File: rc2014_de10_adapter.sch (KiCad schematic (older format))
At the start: 27 parts, among them J1 Conn_02x20_Odd_Even, J2 Conn_01x10_Male, J3 Conn_01x08_Male, J4 M3 Mounting Hole, J5 Z80 Bus, J6 Pro Bus, U1 SN74LVC245A, U10 MAX40200AUK, U2 SN74LVC245A, U3 SN74LVC245A, U4 SN74LVC245A, U5 SN74LVC245A, U6 AZ1117-3.3, U7 MAX40200AUK, U8 MAX40200AUK, U9 MAX40200AUK

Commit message: finished routing
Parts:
- removed C4: 100nF, Capacitor_SMD:C_0805_2012Metric_Pad1.15x1.40mm_HandSolder, symbol Device:C
- removed C6: 1uF, Capacitor_SMD:C_0805_2012Metric_Pad1.15x1.40mm_HandSolder, symbol Device:C
- removed U7, U8: MAX40200AUK, Package_TO_SOT_SMD:SOT-23-5, symbol Analog_Switch:MAX40200AUK
- added C1, C3, C8: 100nF, Capacitor_SMD:C_0805_2012Metric_Pad1.15x1.40mm_HandSolder, symbol Device:C
- C5: value 1uF -> 100nF
- renumbered C9 to C10, C10 to C12, C1 to C4, C3 to C6, C8 to C9, J5 to J1, J6 to J2, J4 to J3, J2 to J4, J1 to J5, J3 to J6, U6 to U1, U9 to U2, U5 to U3, U1 to U4, U2 to U5, U10 to U6, U3 to U7, U4 to U8
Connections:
- net +3V3: now also C4.2, C5.2, C7.2, C3.2, C8.2
- net +5V: now also C1.2; no longer C4.2, C5.2, C7.2
- net A0F: now also J5.7 (Pin_7); no longer J5.28 (Pin_28)
- net A10F: now also J5.15 (Pin_15); no longer J5.23 (Pin_23)
- net A11F: now also J5.16 (Pin_16); no longer J5.21 (Pin_21)
- net A12F: now also J5.13 (Pin_13); no longer J5.19 (Pin_19)
- net A13F: now also J5.14 (Pin_14); no longer J5.17 (Pin_17)
- net A14F: now also J5.9 (Pin_9); no longer J5.15 (Pin_15)
- net A15F: now also J5.10 (Pin_10); no longer J5.13 (Pin_13)
- net A1F: now also J5.8 (Pin_8); no longer J5.26 (Pin_26)
- net A2F: now also J5.5 (Pin_5); no longer J5.24 (Pin_24)
- net A3F: now also J5.6 (Pin_6); no longer J5.22 (Pin_22)
- net A4F: now also J5.3 (Pin_3); no longer J5.20 (Pin_20)
- net A5F: now also J5.4 (Pin_4); no longer J5.18 (Pin_18)
- net A6F: now also J5.1 (Pin_1); no longer J5.16 (Pin_16)
- net A7F: now also J5.2 (Pin_2); no longer J5.14 (Pin_14)
- net A8F: now also J5.17 (Pin_17); no longer J5.27 (Pin_27)
- net A9F: now also J5.18 (Pin_18); no longer J5.25 (Pin_25)
- net CLKF: now also J5.21 (Pin_21); no longer J5.3 (Pin_3)
- net D0F: now also J5.33 (Pin_33); no longer J5.31 (Pin_31)
- net D1F: now also J5.34 (Pin_34); no longer J5.33 (Pin_33)
- net D3F: now also J5.36 (Pin_36); no longer J5.37 (Pin_37)
- net D4F: now also J5.37 (Pin_37); no longer J5.32 (Pin_32)
- net D5F: now also J5.38 (Pin_38); no longer J5.34 (Pin_34)
- net D6F: now also J5.39 (Pin_39); no longer J5.36 (Pin_36)
- net D7F: now also J5.40 (Pin_40); no longer J5.38 (Pin_38)
- net DIR: now also J6.6 (Pin_6); no longer J6.8 (Pin_8)
- net GND: now also J4.4 (Pin_4), C1.1, C3.1, C8.1; no longer J4.7 (Pin_7)
- net PAGE: now also U8.2 (A1); no longer U8.8 (A7)
- net PAGEF: now also J4.5 (Pin_5), U8.18 (B1); no longer J4.9 (Pin_9), U8.12 (B7)
- net RxF: now also J6.7 (Pin_7); no longer J6.1 (Pin_1)
- net TxF: now also J6.8 (Pin_8); no longer J6.2 (Pin_2)
- net ~BUSACKF: now also J6.4 (Pin_4); no longer J5.4 (Pin_4)
- net ~BUSRQ: now also U8.7 (A6); no longer U8.3 (A2)
- net ~BUSRQF: now also J6.2 (Pin_2), U8.13 (B6); no longer J5.8 (Pin_8), U8.17 (B2)
- net ~HALT: now also U8.6 (A5); no longer U8.2 (A1)
- net ~HALTF: now also J6.1 (Pin_1), U8.14 (B5); no longer J5.6 (Pin_6), U8.18 (B1)
- net ~INT: now also U8.3 (A2); no longer U8.6 (A5)
- net ~INTF: now also J4.7 (Pin_7), U8.17 (B2); no longer J5.40 (Pin_40), U8.14 (B5)
- net ~IORQF: now also J5.27 (Pin_27); no longer J5.2 (Pin_2)
- net ~M1F: now also J5.19 (Pin_19); no longer J5.1 (Pin_1)
- net ~MREQF: now also J5.23 (Pin_23); no longer J5.5 (Pin_5)
- net ~NMIF: now also J4.8 (Pin_8); no longer J5.10 (Pin_10)
- net ~RDF: now also J5.24 (Pin_24); no longer J5.9 (Pin_9)
- net ~RESETF: now also J5.22 (Pin_22); no longer J4.10 (Pin_10)
- net ~WAIT: now also U8.8 (A7); no longer U8.7 (A6)
- net ~WAITF: now also J6.3 (Pin_3), U8.12 (B7); no longer J5.39 (Pin_39), U8.13 (B6)
- net ~WRF: now also J5.25 (Pin_25); no longer J5.7 (Pin_7)
- net 5VF: no longer names the net of J5.11 (Pin_11)
- no-connect marks 17 -> 18
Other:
- moved on the sheet: C4, J6

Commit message: Added FTDI header
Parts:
- added J7: FTDI, Connector_PinHeader_2.54mm:PinHeader_1x06_P2.54mm_Horizontal, symbol Connector_Generic:Conn_01x06
- added JP1: Jumper, Connector_PinHeader_2.54mm:PinHeader_1x02_P2.54mm_Vertical, symbol Device:Jumper
- added R1, R2, R3, R4: 2k2, Resistor_SMD:R_0805_2012Metric_Pad1.15x1.40mm_HandSolder, symbol Device:R_Small
- added R5, R6: 100K, Resistor_SMD:R_0805_2012Metric_Pad1.15x1.40mm_HandSolder, symbol Device:R_Small
- J4: symbol Connector:Conn_01x10_Male -> Connector_Generic:Conn_01x10
- J6: symbol Connector:Conn_01x08_Male -> Connector_Generic:Conn_01x08
- U1: MFR (none) -> Diodes Incorporated; MPN (none) -> AZ1117H-3.3TRE1; SPN (none) -> 621-AZ1117H-3.3TRE1; SPR (none) -> Mouser; SPURL (none) -> https://www.mouser.com/ProductDetail/Diodes-Incorporated/AZ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
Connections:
- net +3V3: now also JP1.1, R5.1
- net DIR: now also J6.4 (Pin_4); no longer J6.6 (Pin_6)
- net GND: now also J7.1 (Pin_1), R6.2
- net RxF: now also R1.1
- net TxF: now also R2.1
- net ~BUSACKF: now also J6.2 (Pin_2); no longer J6.4 (Pin_4)
- net ~BUSRQF: now also J4.10 (Pin_10); no longer J6.2 (Pin_2)
- net ~HALTF: now also J4.9 (Pin_9); no longer J6.1 (Pin_1)
- net ~WAITF: now also J6.1 (Pin_1); no longer J6.3 (Pin_3)
- net ~CTSF: now reaches J6.5 (Pin_5)
- net ~CTSF: now also R4.1
- new net: J7.2 (Pin_2), R3.2
- new net: J7.3 (Pin_3), JP1.2
- new net: J7.4 (Pin_4), R1.2, R5.2
- new net: J7.5 (Pin_5), R2.2
- new net: J7.6 (Pin_6), R4.2, R6.1
- new net ~RTSF: J6.6 (Pin_6), R3.1
- no-connect marks 18 -> 16

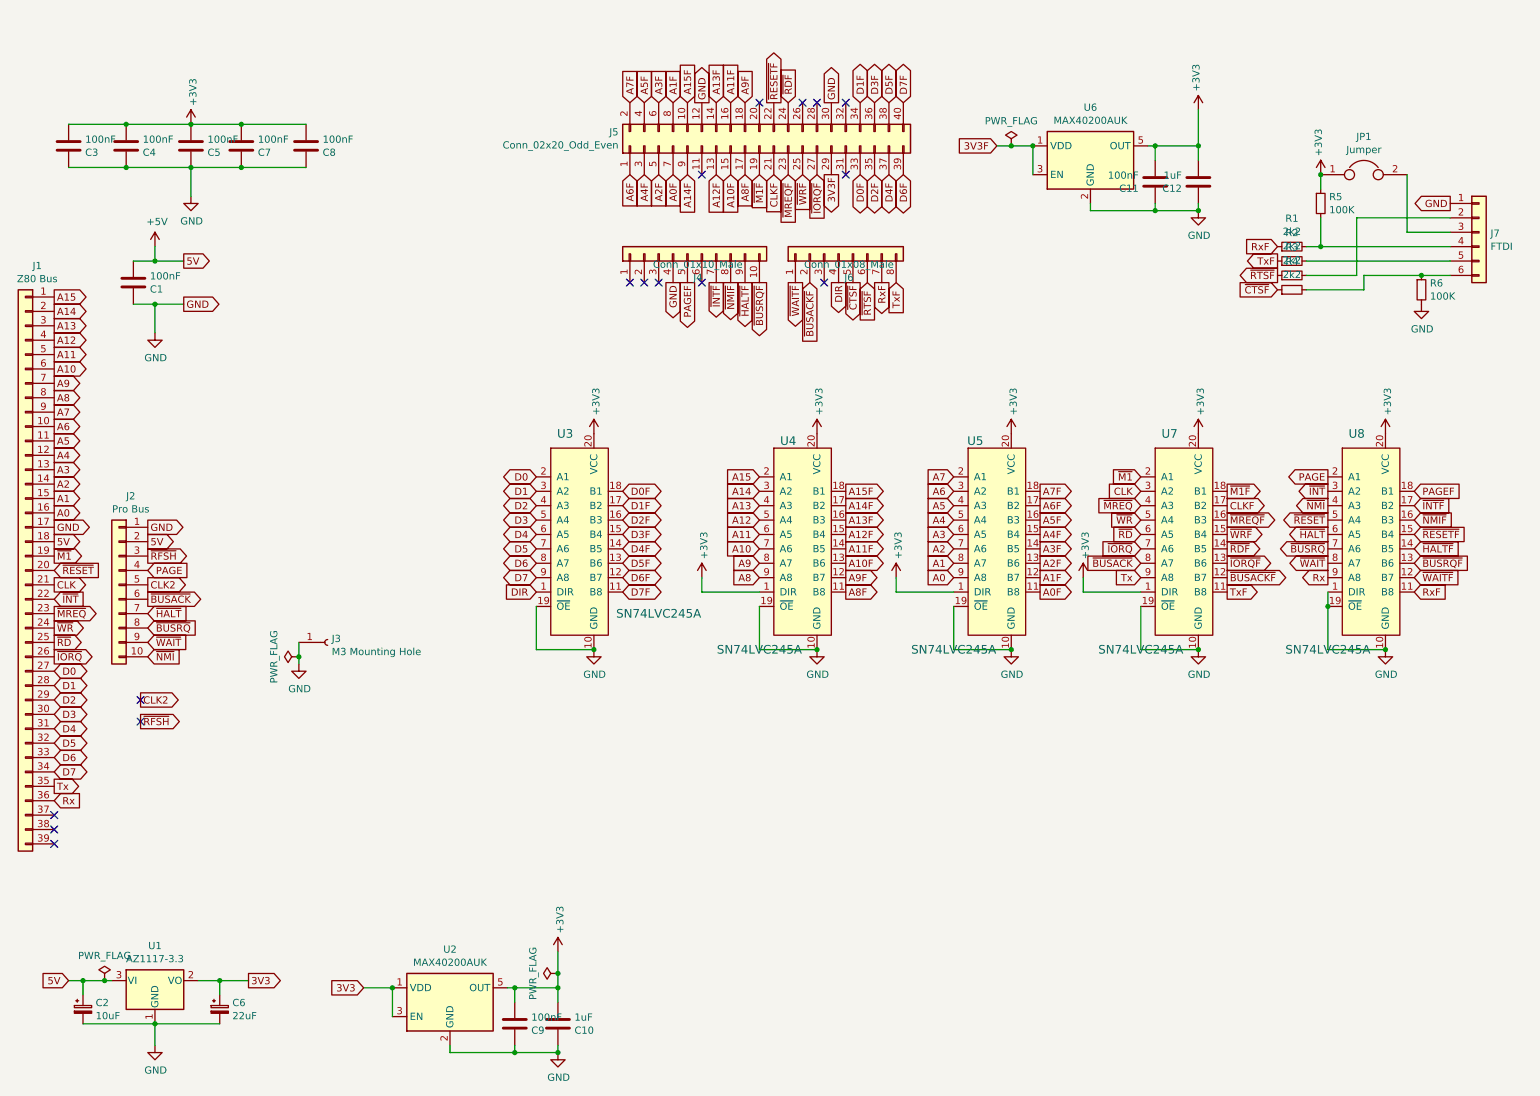
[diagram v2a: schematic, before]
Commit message: added direction flags for bus transceivers
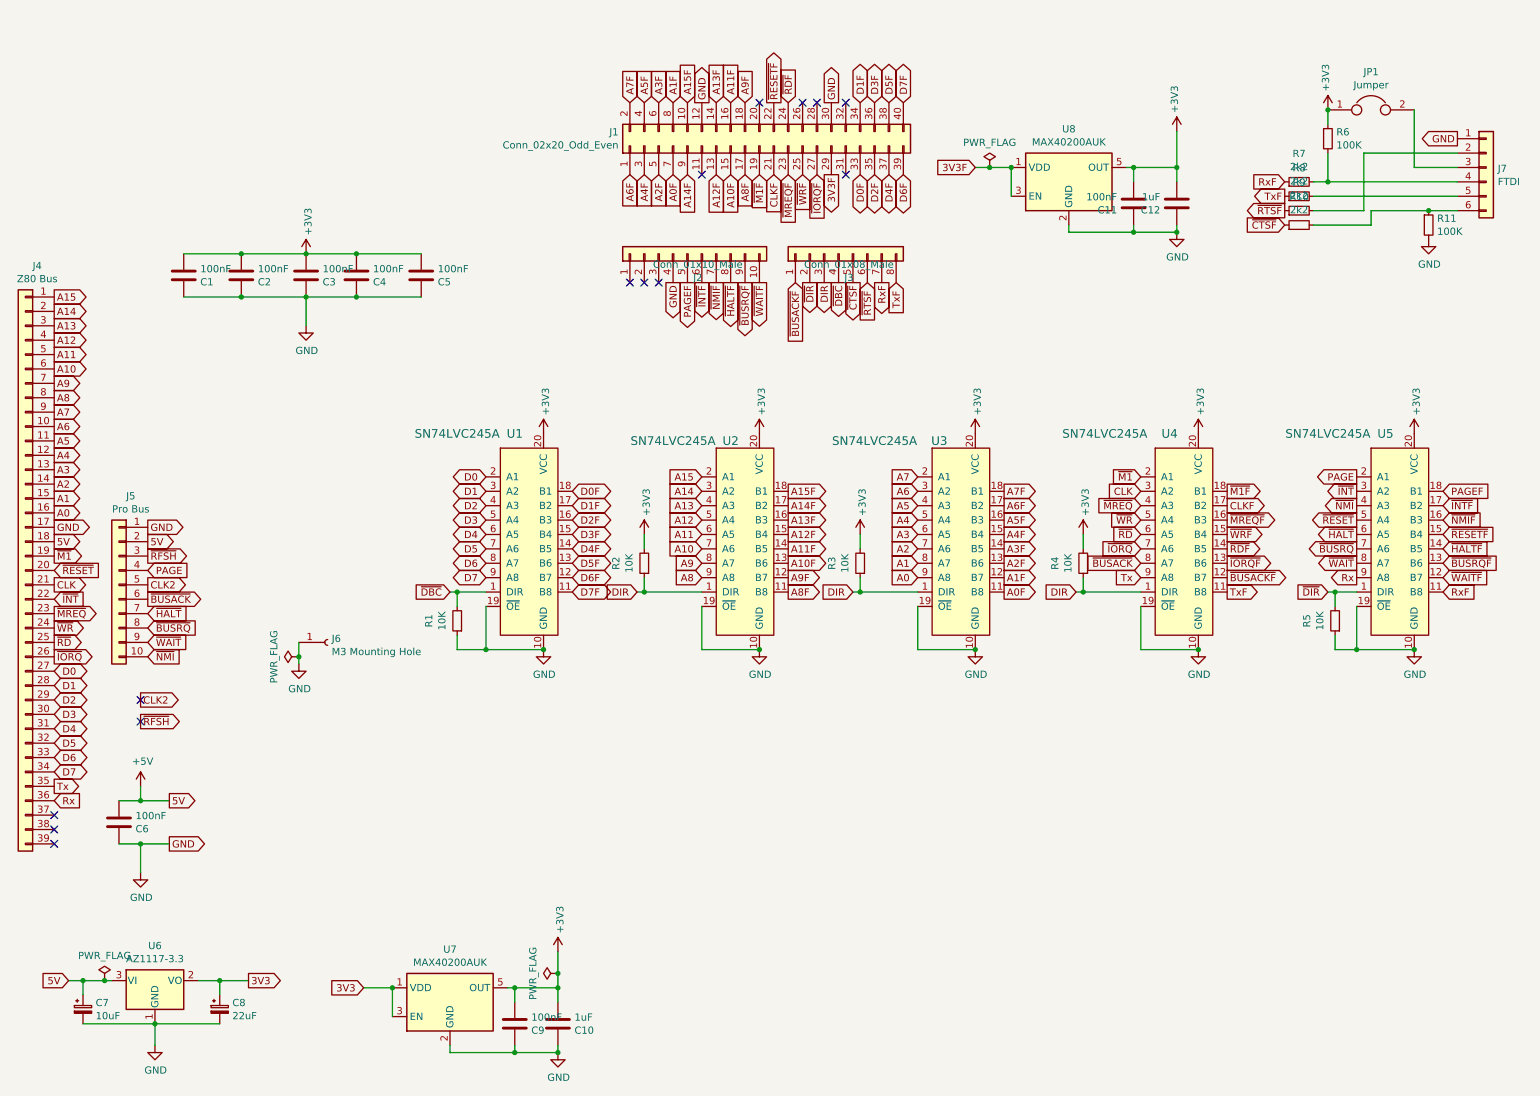
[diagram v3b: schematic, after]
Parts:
- added R1, R2, R3, R4, R5: 10K, Resistor_SMD:R_0805_2012Metric_Pad1.15x1.40mm_HandSolder, symbol Device:R_Small
- renumbered C3 to C1, C4 to C2, C5 to C3, C7 to C4, C8 to C5, C1 to C6, C2 to C7, C6 to C8, J5 to J1, J4 to J2, J6 to J3, J1 to J4, J2 to J5, J3 to J6, R4 to R10, R6 to R11, R5 to R6, R1 to R7, R2 to R8, R3 to R9, U3 to U1, U4 to U2, U5 to U3, U7 to U4, U8 to U5, U1 to U6, U2 to U7, U6 to U8
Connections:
- net +3V3: now also R2.2, R3.2, R4.2; no longer U2.1 (DIR), U3.1 (DIR), U4.1 (DIR)
- net DIR: now also J3.3 (Pin_3), U2.1 (DIR), U3.1 (DIR), U4.1 (DIR), R2.1, R3.1, R4.1; no longer J3.4 (Pin_4), U1.1 (DIR)
- net GND: now also R1.1, R5.1; no longer U5.1 (DIR)
- net ~BUSACKF: now also J3.1 (Pin_1); no longer J3.2 (Pin_2)
- net ~BUSRQF: now also J2.9 (Pin_9); no longer J2.10 (Pin_10)
- net ~HALTF: now also J2.8 (Pin_8); no longer J2.9 (Pin_9)
- net ~INTF: now also J2.6 (Pin_6); no longer J2.7 (Pin_7)
- net ~NMIF: now also J2.7 (Pin_7); no longer J2.8 (Pin_8)
- net ~WAITF: now also J2.10 (Pin_10); no longer J3.1 (Pin_1)
- new net ~DBC: J3.4 (Pin_4), R1.2, U1.1 (DIR)
- new net ~DIR: J3.2 (Pin_2), R5.2, U5.1 (DIR)
- no-connect marks 16 -> 14
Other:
- moved on the sheet: C1, C11, C12, C2, C3, C4, C5, C6, J7, JP1, R10, R11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

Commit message: fix caps on ideal diodes
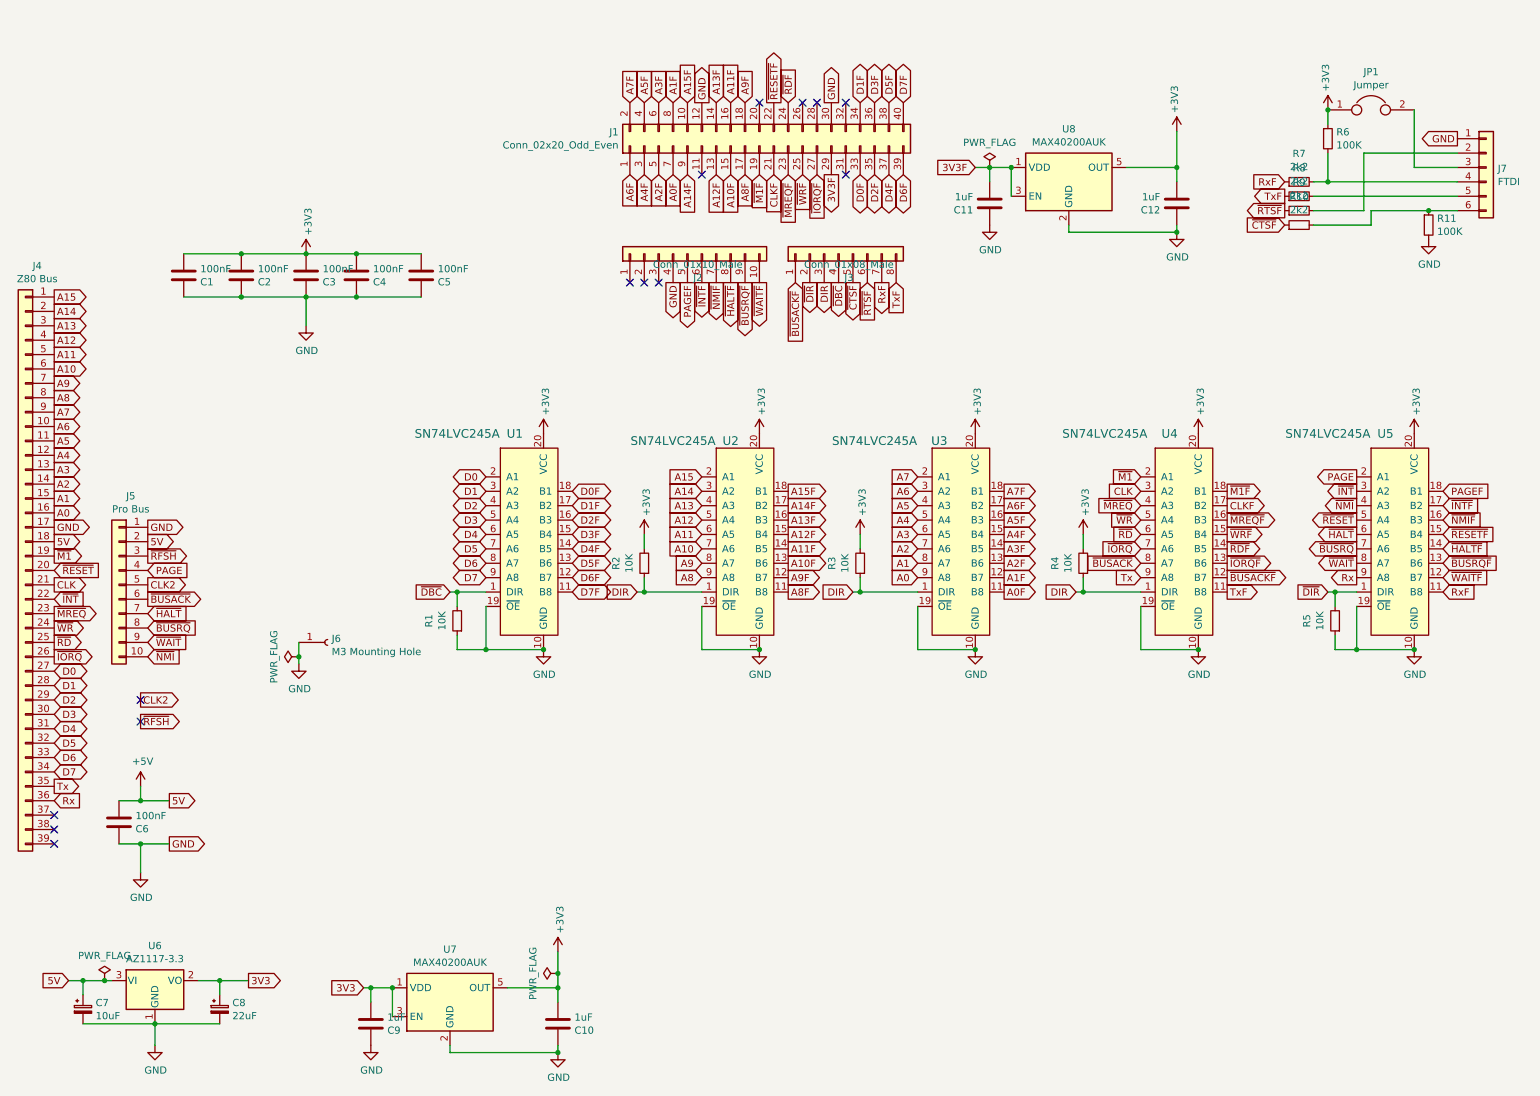
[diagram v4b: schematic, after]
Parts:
- C11, C9: value 100nF -> 1uF
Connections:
- net +3V3: no longer C11.2, C9.2
- net 3V3: now also C9.2
- net 3V3F: now also C11.2
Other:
- moved on the sheet: C11, C9
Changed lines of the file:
@@
 $EndComp
 Wire Wire Line
-	3100 7050 3300 7050
+	3100 7050 3150 7050
 Wire Wire Line
 	7600 1350 7600 1550
@@
 L Device:C C9
 U 1 1 5CD7F41A
-P 4150 7300
-F 0 "C9" H 4265 7346 50  0000 L CNN
-F 1 "100nF" H 4265 7255 50  0000 L CNN
-F 2 "Capacitor_SMD:C_0805_2012Metric_Pad1.15x1.40mm_HandSolder" H 4188 7150 50  0001 C CNN
-F 3 "https://www.mouser.com/datasheet/2/212/KEM_C1002_X7R_SMD-1102033.pdf" H 4150 7300 50  0001 C CNN
-F 4 "KEMET" H -1150 600 50  0001 C CNN "MFR"
-F 5 "C0805C104K4RACTU" H -1150 600 50  0001 C CNN "MPN"
-F 6 "Mouser" H -1150 600 50  0001 C CNN "SPR"
-F 7 "80-C0805C104K4R" H -1150 600 50  0001 C CNN "SPN"
-F 8 "https://www.mouser.com/ProductDetail/KEMET/C0805C104K4RACTU?qs=sGAEpiMZZMs0AnBnWHyRQFCCI5cSbRT%2F1Gdrl2EbPVM%3D" H -1150 600 50  0001 C CNN "SPURL"
-	1    4150 7300
+P 3150 7300
+F 0 "C9" H 3265 7346 50  0000 L CNN
+F 1 "1uF" H 3265 7255 50  0000 L CNN
+F 2 "Capacitor_SMD:C_0805_2012Metric_Pad1.15x1.40mm_HandSolder" H 3188 7150 50  0001 C CNN
+F 3 "https://www.mouser.com/datasheet/2/212/KEM_C1002_X7R_SMD-1102033.pdf" H 3150 7300 50  0001 C CNN
+F 4 "KEMET" H -2150 600 50  0001 C CNN "MFR"
+F 5 "C0805C104K4RACTU" H -2150 600 50  0001 C CNN "MPN"
+F 6 "Mouser" H -2150 600 50  0001 C CNN "SPR"
+F 7 "80-C0805C104K4R" H -2150 600 50  0001 C CNN "SPN"
+F 8 "https://www.mouser.com/ProductDetail/KEMET/C0805C104K4RACTU?qs=sGAEpiMZZMs0AnBnWHyRQFCCI5cSbRT%2F1Gdrl2EbPVM%3D" H -2150 600 50  0001 C CNN "SPURL"
+	1    3150 7300
 	1    0    0    1
 $EndComp
@@
 L Device:C C11
 U 1 1 5CD7F425
-P 8450 1600
-F 0 "C11" H 8565 1646 50  0000 L CNN
-F 1 "100nF" H 8565 1555 50  0000 L CNN
-F 2 "Capacitor_SMD:C_0805_2012Metric_Pad1.15x1.40mm_HandSolder" H 8488 1450 50  0001 C CNN
-F 3 "https://www.mouser.com/datasheet/2/212/KEM_C1002_X7R_SMD-1102033.pdf" H 8450 1600 50  0001 C CNN
-F 4 "KEMET" H 3150 -5100 50  0001 C CNN "MFR"
-F 5 "C0805C104K4RACTU" H 3150 -5100 50  0001 C CNN "MPN"
-F 6 "Mouser" H 3150 -5100 50  0001 C CNN "SPR"
-F 7 "80-C0805C104K4R" H 3150 -5100 50  0001 C CNN "SPN"
-F 8 "https://www.mouser.com/ProductDetail/KEMET/C0805C104K4RACTU?qs=sGAEpiMZZMs0AnBnWHyRQFCCI5cSbRT%2F1Gdrl2EbPVM%3D" H 3150 -5100 50  0001 C CNN "SPURL"
-	1    8450 1600
+P 7450 1600
+F 0 "C11" H 7565 1646 50  0000 L CNN
+F 1 "1uF" H 7565 1555 50  0000 L CNN
+F 2 "Capacitor_SMD:C_0805_2012Metric_Pad1.15x1.40mm_HandSolder" H 7488 1450 50  0001 C CNN
+F 3 "https://www.mouser.com/datasheet/2/212/KEM_C1002_X7R_SMD-1102033.pdf" H 7450 1600 50  0001 C CNN
+F 4 "KEMET" H 2150 -5100 50  0001 C CNN "MFR"
+F 5 "C0805C104K4RACTU" H 2150 -5100 50  0001 C CNN "MPN"
+F 6 "Mouser" H 2150 -5100 50  0001 C CNN "SPR"
+F 7 "80-C0805C104K4R" H 2150 -5100 50  0001 C CNN "SPN"
+F 8 "https://www.mouser.com/ProductDetail/KEMET/C0805C104K4RACTU?qs=sGAEpiMZZMs0AnBnWHyRQFCCI5cSbRT%2F1Gdrl2EbPVM%3D" H 2150 -5100 50  0001 C CNN "SPURL"
+	1    7450 1600
 	-1   0    0    1
 $EndComp
@@
 $EndComp
 Wire Wire Line
-	4100 7050 4150 7050
-Wire Wire Line
 	4450 7150 4450 7050
 Connection ~ 4450 7050
 Wire Wire Line
-	4150 7150 4150 7050
-Connection ~ 4150 7050
-Wire Wire Line
-	4150 7050 4450 7050
-Wire Wire Line
-	8450 1450 8450 1350
-Connection ~ 8450 1350
-Wire Wire Line
-	8450 1350 8400 1350
+	3150 7150 3150 7050
 Wire Wire Line
 	8750 1450 8750 1350
 Connection ~ 8750 1350
 Wire Wire Line
-	8750 1350 8450 1350
-Wire Wire Line
-	3700 7500 4150 7500
-Wire Wire Line
-	4150 7450 4150 7500
-Connection ~ 4150 7500
-Wire Wire Line
-	4150 7500 4450 7500
-Wire Wire Line
 	4450 7450 4450 7500
 Wire Wire Line
 	8750 1750 8750 1800
-Wire Wire Line
-	8750 1800 8450 1800
-Wire Wire Line
-	8450 1750 8450 1800
-Connection ~ 8450 1800
-Wire Wire Line
-	8450 1800 8000 1800
 Connection ~ 4450 7500
 Connection ~ 8750 1800
@@
 	10000 4300 9850 4300
 Connection ~ 9850 4300
+$Comp
+L power:GND #PWR0101
+U 1 1 5CD5A62D
+P 7450 1750
+AR Path="/5CD5A62D" Ref="#PWR0101"  Part="1"
+AR Path="/5CB63856/5CD5A62D" Ref="#PWR?"  Part="1"
+AR Path="/5CB5AB00/5CB63856/5CD5A62D" Ref="#PWR?"  Part="1"
+F 0 "#PWR0101" H 7450 1500 50  0001 C CNN
+F 1 "GND" H 7455 1577 50  0000 C CNN
+F 2 "" H 7450 1750 50  0001 C CNN
+F 3 "" H 7450 1750 50  0001 C CNN
+	1    7450 1750
+	1    0    0    -1
+$EndComp
+Wire Wire Line
+	7450 1450 7450 1350
+Wire Wire Line
+	8400 1350 8750 1350
+Wire Wire Line
+	8000 1800 8750 1800
+Connection ~ 3150 7050
+Wire Wire Line
+	3150 7050 3300 7050
+Wire Wire Line
+	4100 7050 4450 7050
+Wire Wire Line
+	3700 7500 4450 7500
+$Comp
+L power:GND #PWR0102
+U 1 1 5CD69ACB
+P 3150 7450
+AR Path="/5CD69ACB" Ref="#PWR0102"  Part="1"
+AR Path="/5CB63856/5CD69ACB" Ref="#PWR?"  Part="1"
+AR Path="/5CB5AB00/5CB63856/5CD69ACB" Ref="#PWR?"  Part="1"
+F 0 "#PWR0102" H 3150 7200 50  0001 C CNN
+F 1 "GND" H 3155 7277 50  0000 C CNN
+F 2 "" H 3150 7450 50  0001 C CNN
+F 3 "" H 3150 7450 50  0001 C CNN
+	1    3150 7450
+	1    0    0    -1
+$EndComp
 $EndSCHEMATC
